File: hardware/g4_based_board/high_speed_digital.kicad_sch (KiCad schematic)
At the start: 52 parts, among them J11 Conn_01x06_Pin, J16 Conn_01x09, J6 Conn_01x04, Q3 PMOS, Q4 PMOS, U10 TCA9800, U11 TCA9800, U2 MCP9804_MSOP, U3 MCP3428x-xST, U8 BME680

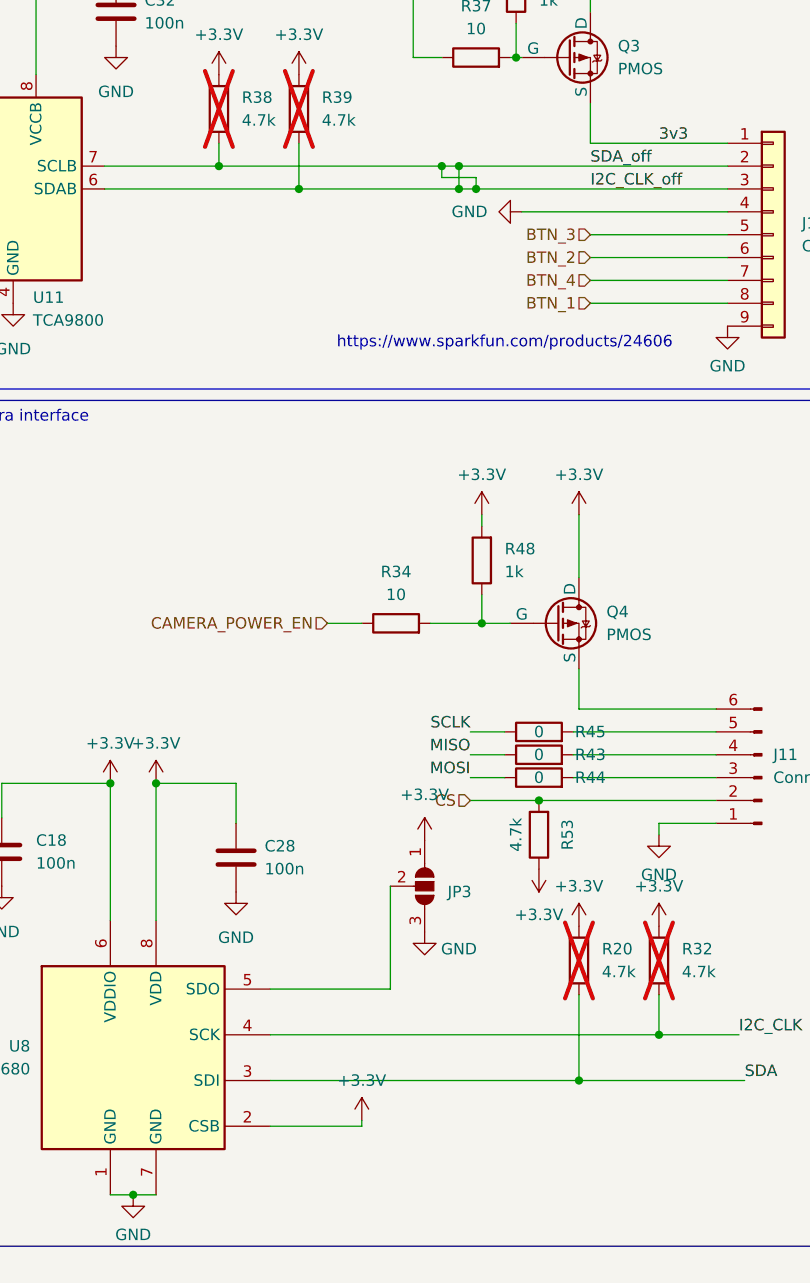
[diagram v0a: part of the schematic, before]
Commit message: fixed a minor error in the sch
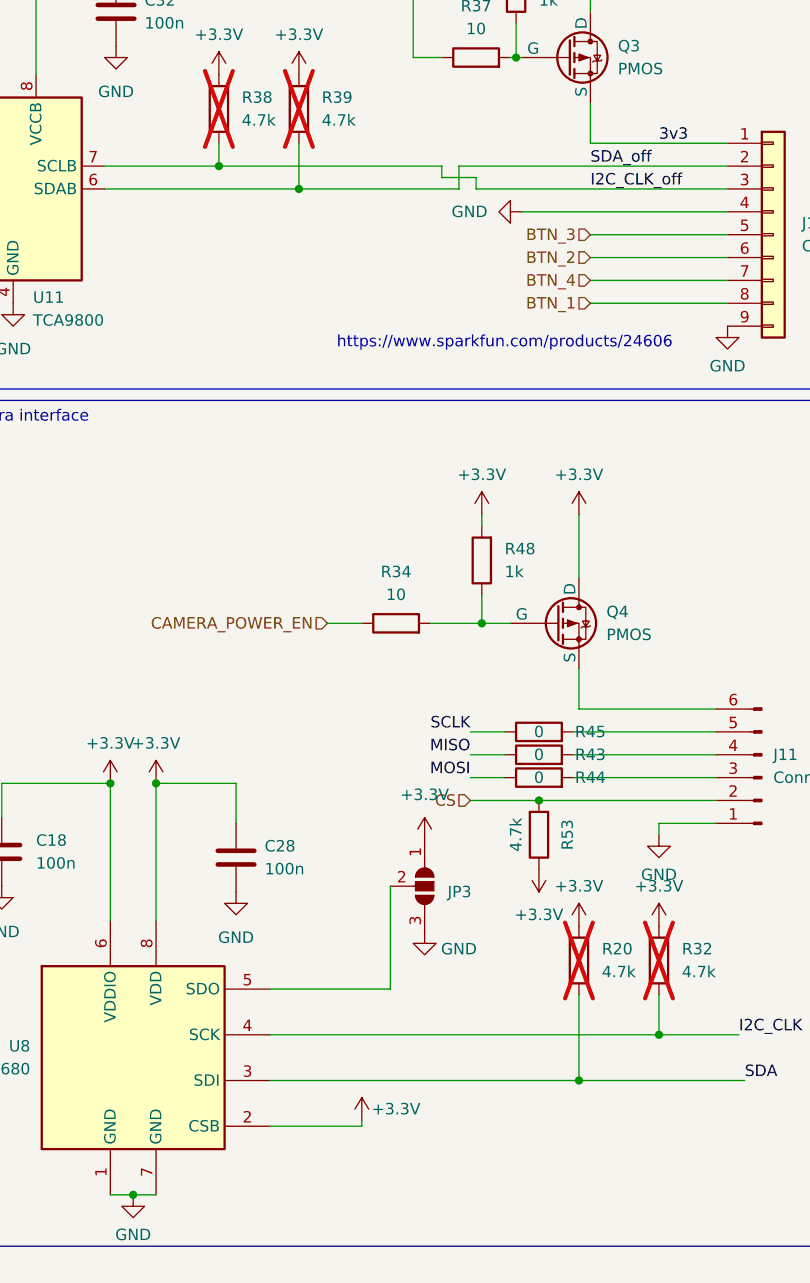
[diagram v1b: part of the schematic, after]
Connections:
- net I2C_CLK_off: no longer J16.2 (Pin_2), R39.2, U11.6 (SDAB)
- new net SDA_off: J16.2 (Pin_2), R39.2, U11.6 (SDAB)
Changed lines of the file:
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@@
 	)
 	(junction
-		(at 234.315 48.26)
-		(diameter 0)
-		(color 0 0 0 0)
-	)
-	(junction
 		(at 32.385 31.75)
 		(diameter 0)
@@
 	)
 	(junction
-		(at 230.505 45.72)
-		(diameter 0)
-		(color 0 0 0 0)
-	)
-	(junction
-		(at 232.41 48.26)
-		(diameter 0)
-		(color 0 0 0 0)
-	)
-	(junction
 		(at 85.09 87.63)
 		(diameter 0)
@@
 	)
 	(junction
-		(at 232.41 45.72)
-		(diameter 0)
-		(color 0 0 0 0)
-	)
-	(junction
 		(at 214.63 48.26)
 		(diameter 0)
@@
 	(wire
 		(pts
-			(xy 234.315 48.26) (xy 232.41 48.26)
-		)
-		(stroke
-			(width 0)
-			(type default)
-		)
-	)
-	(wire
-		(pts
 			(xy 232.41 48.26) (xy 214.63 48.26)
 		)
@@
 	(wire
 		(pts
-			(xy 232.41 45.72) (xy 230.505 45.72)
-		)
-		(stroke
-			(width 0)
-			(type default)
-		)
-	)
-	(wire
-		(pts
 			(xy 233.68 108.585) (xy 237.49 108.585)
 		)
@@
 		(on_board yes)
 		(dnp no)
-		(fields_autoplaced yes)
 		(property "Reference" "#PWR0118"
 			(at 221.615 155.575 0)
@@
 		)
 		(property "Value" "+3.3V"
-			(at 221.615 147.32 0)
+			(at 225.425 150.495 0)
 			(effects
 				(font
